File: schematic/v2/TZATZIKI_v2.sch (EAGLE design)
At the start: 3 parts, among them J1 2X20-CHIP-HEADERS2X20CHIP_OFF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, J2 USD-SDIO-SOCKET

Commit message: added fourway version
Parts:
- added POWER_USB: USBUSB-MICROB-SMT-DIP, Spark:USBUSB-MICROB-SMT-DIP
- added SDIO_TOP, SPI_BOT, SPI_TOP: USD-SDIO-SOCKET, JKW_CHIP:USD-SDIO-SOCKET
- renumbered J2 to SDIO_BOT
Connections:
- removed net N$1: J1.ACIN-5V
- new net N$11: J1.CSIPCK/CS0, SPI_BOT.CD/DAT3, SPI_TOP.CD/DAT3
- new net N$12: J1.HSY/MOSI, SPI_BOT.CMD, SPI_TOP.CMD
- new net N$13: J1.VSY/MISO, SPI_BOT.DAT0, SPI_TOP.DAT0
- new net N$14: J1.CSICK/CLK, SPI_BOT.CLK, SPI_TOP.CLK
- new net VOUT: J1.ACIN-5V, POWER_USB.VBUS
- net GND: now also POWER_USB.GND, SDIO_TOP.CD1, SDIO_TOP.CD2, SDIO_TOP.GND, SDIO_TOP.SHIELD@1, SDIO_TOP.SHIELD@3, SPI_BOT.CD1, SPI_BOT.CD2, SPI_BOT.GND, SPI_BOT.SHIELD@1, SPI_BOT.SHIELD@3, SPI_TOP.CD1, SPI_TOP.CD2, SPI_TOP.GND, SPI_TOP.SHIELD@1, SPI_TOP.SHIELD@3
- net N$10: now also SDIO_TOP.VCC, SPI_BOT.VCC, SPI_TOP.VCC
- net N$2: now also SDIO_TOP.CD/DAT3
- net N$3: now also SDIO_TOP.DAT0
- net N$4: now also SDIO_TOP.CMD
- net N$5: now also SDIO_TOP.CLK
- net N$6: now also SDIO_TOP.DAT1
- net N$9: now also SDIO_TOP.DAT2
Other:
- note added: "clk"
- note added: "cs"
- note added: "di"
- note added: "do"
- note added: "x"

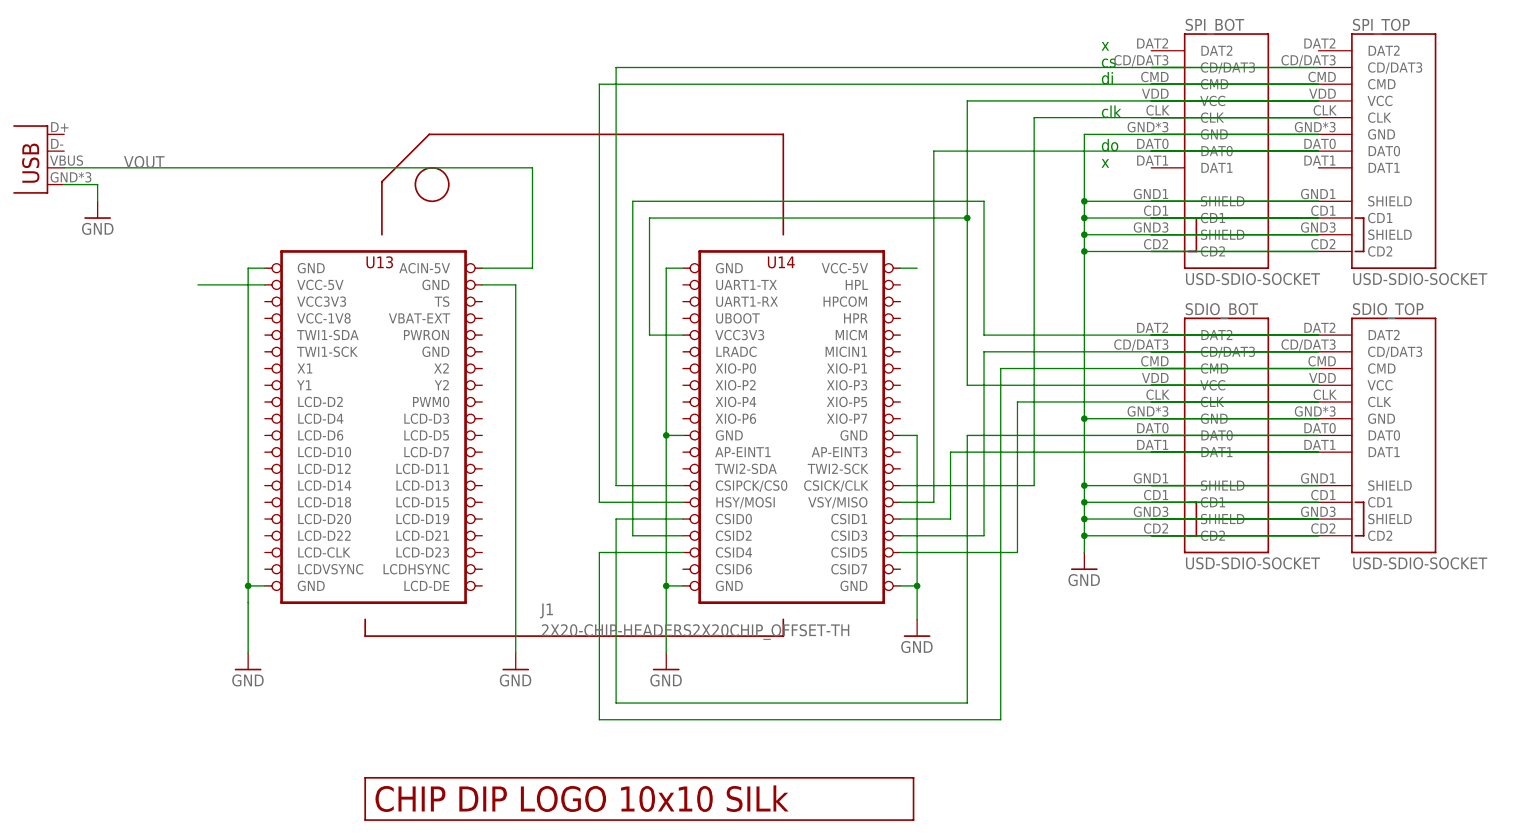
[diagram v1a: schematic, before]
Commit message: added v4 with card detect pin
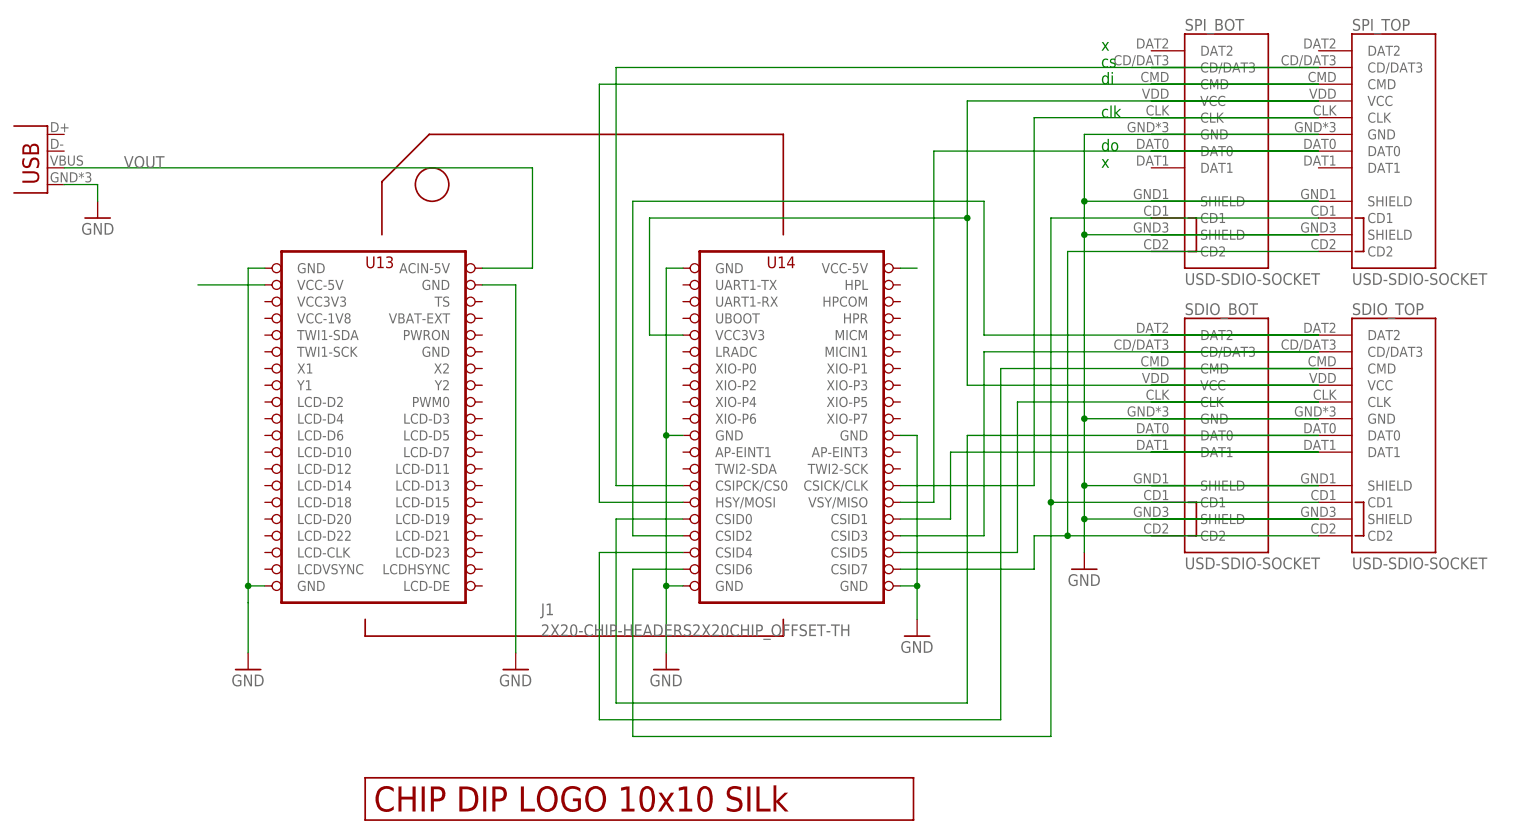
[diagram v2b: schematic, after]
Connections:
- new net N$1: J1.CSID7, SDIO_BOT.CD2, SDIO_TOP.CD2, SPI_BOT.CD2, SPI_TOP.CD2
- new net N$19: J1.CSID6, SDIO_BOT.CD1, SDIO_TOP.CD1, SPI_BOT.CD1, SPI_TOP.CD1
- net GND: no longer SDIO_BOT.CD1, SDIO_BOT.CD2, SDIO_TOP.CD1, SDIO_TOP.CD2, SPI_BOT.CD1, SPI_BOT.CD2, SPI_TOP.CD1, SPI_TOP.CD2
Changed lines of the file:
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@@
 <pinref part="GND2" gate="1" pin="GND"/>
 <wire x1="172.72" y1="30.48" x2="137.16" y2="30.48" width="0.1524" layer="91"/>
-<wire x1="137.16" y1="30.48" x2="137.16" y2="27.94" width="0.1524" layer="91"/>
 <pinref part="SDIO_BOT" gate="G$1" pin="SHIELD@3"/>
-<wire x1="137.16" y1="27.94" x2="137.16" y2="25.4" width="0.1524" layer="91"/>
-<wire x1="137.16" y1="22.86" x2="137.16" y2="20.32" width="0.1524" layer="91"/>
+<wire x1="137.16" y1="30.48" x2="137.16" y2="25.4" width="0.1524" layer="91"/>
 <wire x1="172.72" y1="25.4" x2="137.16" y2="25.4" width="0.1524" layer="91"/>
 <pinref part="SDIO_BOT" gate="G$1" pin="GND"/>
@@
 <junction x="137.16" y="25.4"/>
 <junction x="137.16" y="30.48"/>
-<pinref part="SDIO_BOT" gate="G$1" pin="CD1"/>
-<wire x1="172.72" y1="27.94" x2="137.16" y2="27.94" width="0.1524" layer="91"/>
-<pinref part="SDIO_BOT" gate="G$1" pin="CD2"/>
-<wire x1="137.16" y1="25.4" x2="137.16" y2="22.86" width="0.1524" layer="91"/>
-<wire x1="137.16" y1="22.86" x2="172.72" y2="22.86" width="0.1524" layer="91"/>
-<junction x="137.16" y="22.86"/>
-<junction x="137.16" y="27.94"/>
+<wire x1="137.16" y1="25.4" x2="137.16" y2="20.32" width="0.1524" layer="91"/>
 <pinref part="SPI_BOT" gate="G$1" pin="GND"/>
 <wire x1="172.72" y1="83.82" x2="137.16" y2="83.82" width="0.1524" layer="91"/>
 <wire x1="137.16" y1="83.82" x2="137.16" y2="73.66" width="0.1524" layer="91"/>
-<wire x1="137.16" y1="73.66" x2="137.16" y2="71.12" width="0.1524" layer="91"/>
-<wire x1="137.16" y1="71.12" x2="137.16" y2="68.58" width="0.1524" layer="91"/>
-<wire x1="137.16" y1="68.58" x2="137.16" y2="66.04" width="0.1524" layer="91"/>
-<wire x1="137.16" y1="40.64" x2="137.16" y2="66.04" width="0.1524" layer="91"/>
-<pinref part="SPI_BOT" gate="G$1" pin="CD2"/>
-<wire x1="137.16" y1="66.04" x2="172.72" y2="66.04" width="0.1524" layer="91"/>
+<wire x1="137.16" y1="73.66" x2="137.16" y2="68.58" width="0.1524" layer="91"/>
+<wire x1="137.16" y1="40.64" x2="137.16" y2="68.58" width="0.1524" layer="91"/>
 <pinref part="SPI_BOT" gate="G$1" pin="SHIELD@3"/>
 <wire x1="172.72" y1="68.58" x2="137.16" y2="68.58" width="0.1524" layer="91"/>
-<pinref part="SPI_BOT" gate="G$1" pin="CD1"/>
-<wire x1="172.72" y1="71.12" x2="137.16" y2="71.12" width="0.1524" layer="91"/>
 <pinref part="SPI_BOT" gate="G$1" pin="SHIELD@1"/>
 <wire x1="172.72" y1="73.66" x2="137.16" y2="73.66" width="0.1524" layer="91"/>
-<junction x="137.16" y="66.04"/>
 <junction x="137.16" y="68.58"/>
-<junction x="137.16" y="71.12"/>
 <junction x="137.16" y="73.66"/>
 <junction x="137.16" y="40.64"/>
@@
 <pinref part="SPI_TOP" gate="G$1" pin="SHIELD@3"/>
 <pinref part="SPI_TOP" gate="G$1" pin="SHIELD@1"/>
-<pinref part="SPI_TOP" gate="G$1" pin="CD1"/>
-<pinref part="SPI_TOP" gate="G$1" pin="CD2"/>
 <pinref part="SDIO_TOP" gate="G$1" pin="GND"/>
 <pinref part="SDIO_TOP" gate="G$1" pin="SHIELD@3"/>
 <pinref part="SDIO_TOP" gate="G$1" pin="SHIELD@1"/>
-<pinref part="SDIO_TOP" gate="G$1" pin="CD1"/>
-<pinref part="SDIO_TOP" gate="G$1" pin="CD2"/>
-<wire x1="172.72" y1="27.94" x2="147.32" y2="27.94" width="0.1524" layer="91"/>
-<wire x1="172.72" y1="22.86" x2="147.32" y2="22.86" width="0.1524" layer="91"/>
 <wire x1="172.72" y1="30.48" x2="147.32" y2="30.48" width="0.1524" layer="91"/>
 <wire x1="172.72" y1="40.64" x2="147.32" y2="40.64" width="0.1524" layer="91"/>
@@
 <wire x1="172.72" y1="68.58" x2="147.32" y2="68.58" width="0.1524" layer="91"/>
 <wire x1="172.72" y1="83.82" x2="147.32" y2="83.82" width="0.1524" layer="91"/>
-<wire x1="172.72" y1="71.12" x2="147.32" y2="71.12" width="0.1524" layer="91"/>
-<wire x1="172.72" y1="66.04" x2="147.32" y2="66.04" width="0.1524" layer="91"/>
 <wire x1="172.72" y1="73.66" x2="147.32" y2="73.66" width="0.1524" layer="91"/>
 </segment>
@@
 </segment>
 </net>
+<net name="N$1" class="0">
+<segment>
+<pinref part="SPI_BOT" gate="G$1" pin="CD2"/>
+<pinref part="SPI_TOP" gate="G$1" pin="CD2"/>
+<wire x1="172.72" y1="66.04" x2="147.32" y2="66.04" width="0.1524" layer="91"/>
+<pinref part="SDIO_BOT" gate="G$1" pin="CD2"/>
+<pinref part="SDIO_TOP" gate="G$1" pin="CD2"/>
+<wire x1="172.72" y1="22.86" x2="147.32" y2="22.86" width="0.1524" layer="91"/>
+<pinref part="J1" gate="G$1" pin="CSID7"/>
+<wire x1="109.22" y1="17.78" x2="129.54" y2="17.78" width="0.1524" layer="91"/>
+<wire x1="129.54" y1="17.78" x2="129.54" y2="22.86" width="0.1524" layer="91"/>
+<wire x1="129.54" y1="22.86" x2="134.62" y2="22.86" width="0.1524" layer="91"/>
+<wire x1="134.62" y1="22.86" x2="147.32" y2="22.86" width="0.1524" layer="91"/>
+<wire x1="147.32" y1="66.04" x2="134.62" y2="66.04" width="0.1524" layer="91"/>
+<wire x1="134.62" y1="66.04" x2="134.62" y2="22.86" width="0.1524" layer="91"/>
+<junction x="134.62" y="22.86"/>
+</segment>
+</net>
+<net name="N$19" class="0">
+<segment>
+<pinref part="J1" gate="G$1" pin="CSID6"/>
+<wire x1="76.2" y1="17.78" x2="68.58" y2="17.78" width="0.1524" layer="91"/>
+<wire x1="68.58" y1="17.78" x2="68.58" y2="-7.62" width="0.1524" layer="91"/>
+<wire x1="68.58" y1="-7.62" x2="132.08" y2="-7.62" width="0.1524" layer="91"/>
+<wire x1="132.08" y1="-7.62" x2="132.08" y2="27.94" width="0.1524" layer="91"/>
+<pinref part="SDIO_BOT" gate="G$1" pin="CD1"/>
+<pinref part="SDIO_TOP" gate="G$1" pin="CD1"/>
+<wire x1="172.72" y1="27.94" x2="147.32" y2="27.94" width="0.1524" layer="91"/>
+<wire x1="147.32" y1="27.94" x2="132.08" y2="27.94" width="0.1524" layer="91"/>
+<wire x1="132.08" y1="27.94" x2="132.08" y2="71.12" width="0.1524" layer="91"/>
+<pinref part="SPI_BOT" gate="G$1" pin="CD1"/>
+<pinref part="SPI_TOP" gate="G$1" pin="CD1"/>
+<wire x1="172.72" y1="71.12" x2="147.32" y2="71.12" width="0.1524" layer="91"/>
+<wire x1="132.08" y1="71.12" x2="147.32" y2="71.12" width="0.1524" layer="91"/>
+<junction x="132.08" y="27.94"/>
+</segment>
+</net>
